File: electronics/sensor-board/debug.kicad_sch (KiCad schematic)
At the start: 0 parts

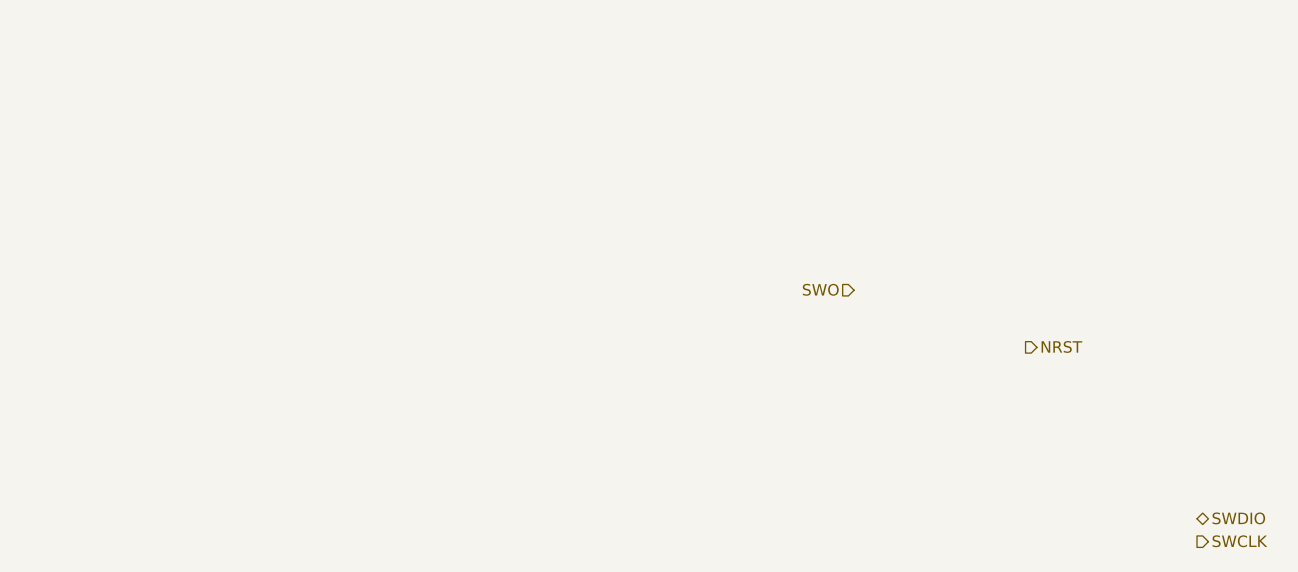
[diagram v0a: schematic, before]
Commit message: LED output, debug and minor controller changes
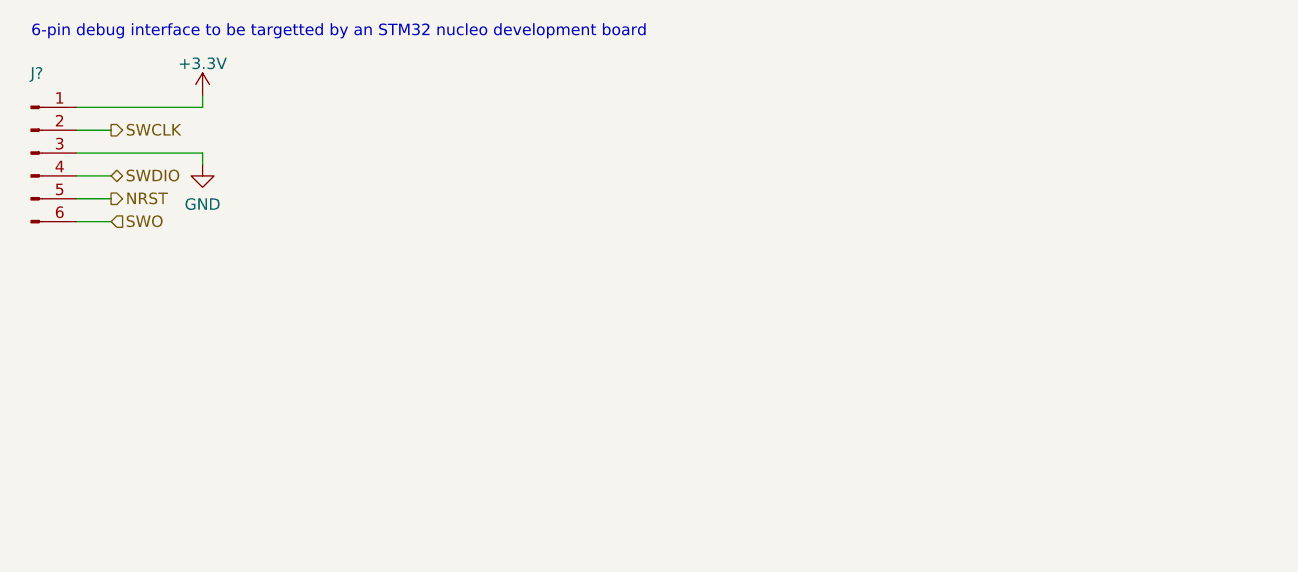
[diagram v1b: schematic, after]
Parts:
- added J?: Conn_01x06_Male, symbol Connector:Conn_01x06_Male
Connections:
- net NRST: now also J?.5 (Pin_5)
- net SWCLK: now also J?.2 (Pin_2)
- net SWDIO: now also J?.4 (Pin_4)
- net SWO: now also J?.6 (Pin_6)
- new net +3.3V: J?.1 (Pin_1)
- new net GND: J?.3 (Pin_3)
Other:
- note added: "6-pin debug interface to be targetted by an STM32 nucleo development board"
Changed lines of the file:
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@@
 (kicad_sch (version 20211123) (generator eeschema)
   (paper "A4")
-  (hierarchical_label "NRST" (shape output) (at 128.27 50.8 0)
+  (wire (pts (xy 22.86 29.21) (xy 36.83 29.21))
+    (stroke (width 0) (type default) (color 0 0 0 0))
+  )
+  (wire (pts (xy 36.83 29.21) (xy 36.83 30.48))
+    (stroke (width 0) (type default) (color 0 0 0 0))
+  )
+  (wire (pts (xy 22.86 24.13) (xy 36.83 24.13))
+    (stroke (width 0) (type default) (color 0 0 0 0))
+  )
+  (wire (pts (xy 22.86 31.75) (xy 26.67 31.75))
+    (stroke (width 0) (type default) (color 0 0 0 0))
+  )
+  (wire (pts (xy 22.86 36.83) (xy 26.67 36.83))
+    (stroke (width 0) (type default) (color 0 0 0 0))
+  )
+  (wire (pts (xy 36.83 24.13) (xy 36.83 22.86))
+    (stroke (width 0) (type default) (color 0 0 0 0))
+  )
+  (wire (pts (xy 22.86 34.29) (xy 26.67 34.29))
+    (stroke (width 0) (type default) (color 0 0 0 0))
+  )
+  (wire (pts (xy 22.86 26.67) (xy 26.67 26.67))
+    (stroke (width 0) (type default) (color 0 0 0 0))
+  )
+  (text "6-pin debug interface to be targetted by an STM32 nucleo development board"
+    (at 17.78 16.51 0)
+    (effects (font (size 1.27 1.27)) (justify left bottom))
+  )
+  (hierarchical_label "NRST" (shape output) (at 26.67 34.29 0)
     (effects (font (size 1.27 1.27)) (justify left))
   )
-  (hierarchical_label "SWO" (shape input) (at 109.22 44.45 180)
-    (effects (font (size 1.27 1.27)) (justify right))
-  )
-  (hierarchical_label "SWCLK" (shape output) (at 147.32 72.39 0)
+  (hierarchical_label "SWO" (shape input) (at 26.67 36.83 0)
     (effects (font (size 1.27 1.27)) (justify left))
   )
-  (hierarchical_label "SWDIO" (shape bidirectional) (at 147.32 69.85 0)
+  (hierarchical_label "SWCLK" (shape output) (at 26.67 26.67 0)
     (effects (font (size 1.27 1.27)) (justify left))
   )
+  (hierarchical_label "SWDIO" (shape bidirectional) (at 26.67 31.75 0)
+    (effects (font (size 1.27 1.27)) (justify left))
+  )
+  (symbol (lib_id "power:GND") (at 36.83 30.48 0) (unit 1)
+    (in_bom yes) (on_board yes) (fields_autoplaced)
+    (property "Reference" "#PWR?" (id 0) (at 36.83 36.83 0)
+      (effects (font (size 1.27 1.27)) hide)
+    )
+    (property "Value" "GND" (id 1) (at 36.83 34.9234 0))
+    (property "Footprint" "" (id 2) (at 36.83 30.48 0)
+      (effects (font (size 1.27 1.27)) hide)
+    )
+    (property "Datasheet" "" (id 3) (at 36.83 30.48 0)
+      (effects (font (size 1.27 1.27)) hide)
+    )
+    (pin "1")
+  )
+  (symbol (lib_id "Connector:Conn_01x06_Male") (at 17.78 29.21 0) (unit 1)
+    (in_bom yes) (on_board yes) (fields_autoplaced)
+    (property "Reference" "J?" (id 0) (at 18.415 20.354 0))
+    (property "Value" "Conn_01x06_Male" (id 1) (at 18.415 22.8909 0)
+      (effects (font (size 1.27 1.27)) hide)
+    )
+    (property "Footprint" "" (id 2) (at 17.78 29.21 0)
+      (effects (font (size 1.27 1.27)) hide)
+    )
+    (property "Datasheet" "~" (id 3) (at 17.78 29.21 0)
+      (effects (font (size 1.27 1.27)) hide)
+    )
+    (pin "1")
+    (pin "2")
+    (pin "3")
+    (pin "4")
+    (pin "5")
+    (pin "6")
+  )
+  (symbol (lib_id "power:+3.3V") (at 36.83 22.86 0) (unit 1)
+    (in_bom yes) (on_board yes) (fields_autoplaced)
+    (property "Reference" "#PWR?" (id 0) (at 36.83 26.67 0)
+      (effects (font (size 1.27 1.27)) hide)
+    )
+    (property "Value" "+3.3V" (id 1) (at 36.83 19.2842 0))
+    (property "Footprint" "" (id 2) (at 36.83 22.86 0)
+      (effects (font (size 1.27 1.27)) hide)
+    )
+    (property "Datasheet" "" (id 3) (at 36.83 22.86 0)
+      (effects (font (size 1.27 1.27)) hide)
+    )
+    (pin "1")
+  )
 )

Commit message: Build Pad Bus and annotate
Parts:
- gave numbers to parts that had none: 1
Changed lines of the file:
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@@
   (symbol (lib_id "power:GND") (at 36.83 30.48 0) (unit 1)
     (in_bom yes) (on_board yes) (fields_autoplaced)
-    (property "Reference" "#PWR?" (id 0) (at 36.83 36.83 0)
+    (property "Reference" "#PWR0100" (id 0) (at 36.83 36.83 0)
       (effects (font (size 1.27 1.27)) hide)
     )
@@
   (symbol (lib_id "Connector:Conn_01x06_Male") (at 17.78 29.21 0) (unit 1)
     (in_bom yes) (on_board yes) (fields_autoplaced)
-    (property "Reference" "J?" (id 0) (at 18.415 20.354 0))
+    (property "Reference" "J17" (id 0) (at 18.415 20.354 0))
     (property "Value" "Conn_01x06_Male" (id 1) (at 18.415 22.8909 0)
       (effects (font (size 1.27 1.27)) hide)
@@
   (symbol (lib_id "power:+3.3V") (at 36.83 22.86 0) (unit 1)
     (in_bom yes) (on_board yes) (fields_autoplaced)
-    (property "Reference" "#PWR?" (id 0) (at 36.83 26.67 0)
+    (property "Reference" "#PWR099" (id 0) (at 36.83 26.67 0)
       (effects (font (size 1.27 1.27)) hide)
     )

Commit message: Minor tweaks, footprints added
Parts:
- J17: footprint (none) -> Connector_PinHeader_2.54mm:PinHeader_1x06_P2.54mm_Vertical
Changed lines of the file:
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@@
       (effects (font (size 1.27 1.27)) hide)
     )
-    (property "Footprint" "" (id 2) (at 17.78 29.21 0)
+    (property "Footprint" "Connector_PinHeader_2.54mm:PinHeader_1x06_P2.54mm_Vertical" (id 2) (at 17.78 29.21 0)
       (effects (font (size 1.27 1.27)) hide)
     )

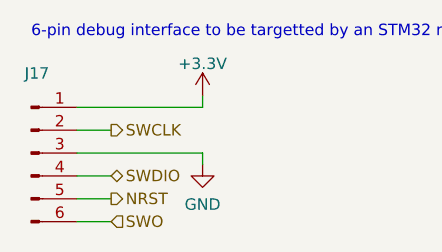
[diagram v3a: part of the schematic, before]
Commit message: Update reference designators
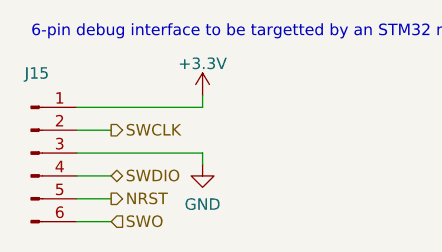
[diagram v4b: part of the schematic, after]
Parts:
- renumbered J17 to J15
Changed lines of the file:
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@@
   (symbol (lib_id "power:GND") (at 36.83 30.48 0) (unit 1)
     (in_bom yes) (on_board yes) (fields_autoplaced)
-    (property "Reference" "#PWR0100" (id 0) (at 36.83 36.83 0)
+    (property "Reference" "#PWR092" (id 0) (at 36.83 36.83 0)
       (effects (font (size 1.27 1.27)) hide)
     )
@@
   (symbol (lib_id "Connector:Conn_01x06_Male") (at 17.78 29.21 0) (unit 1)
     (in_bom yes) (on_board yes) (fields_autoplaced)
-    (property "Reference" "J17" (id 0) (at 18.415 20.354 0))
+    (property "Reference" "J15" (id 0) (at 18.415 20.354 0))
     (property "Value" "Conn_01x06_Male" (id 1) (at 18.415 22.8909 0)
       (effects (font (size 1.27 1.27)) hide)
@@
   (symbol (lib_id "power:+3.3V") (at 36.83 22.86 0) (unit 1)
     (in_bom yes) (on_board yes) (fields_autoplaced)
-    (property "Reference" "#PWR099" (id 0) (at 36.83 26.67 0)
+    (property "Reference" "#PWR091" (id 0) (at 36.83 26.67 0)
       (effects (font (size 1.27 1.27)) hide)
     )
